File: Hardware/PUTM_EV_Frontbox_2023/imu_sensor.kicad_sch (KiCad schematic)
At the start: 21 parts, among them J5 Conn_01x06, J6 Conn_01x05, J7 Conn_01x02, J8 Conn_01x02, U17 IMS330DHCX, U2 AS5600

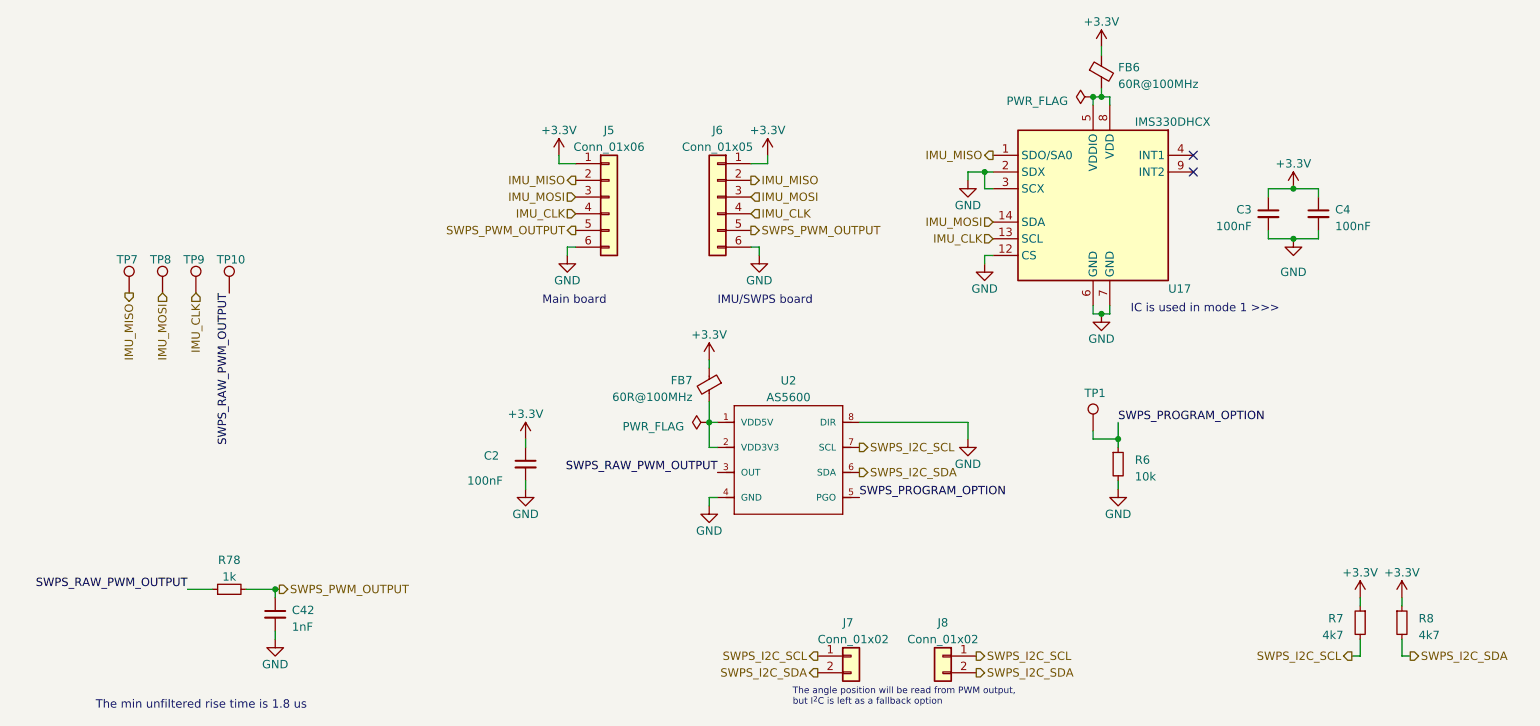
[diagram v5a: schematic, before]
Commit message: Schematic modified, footprints assigned
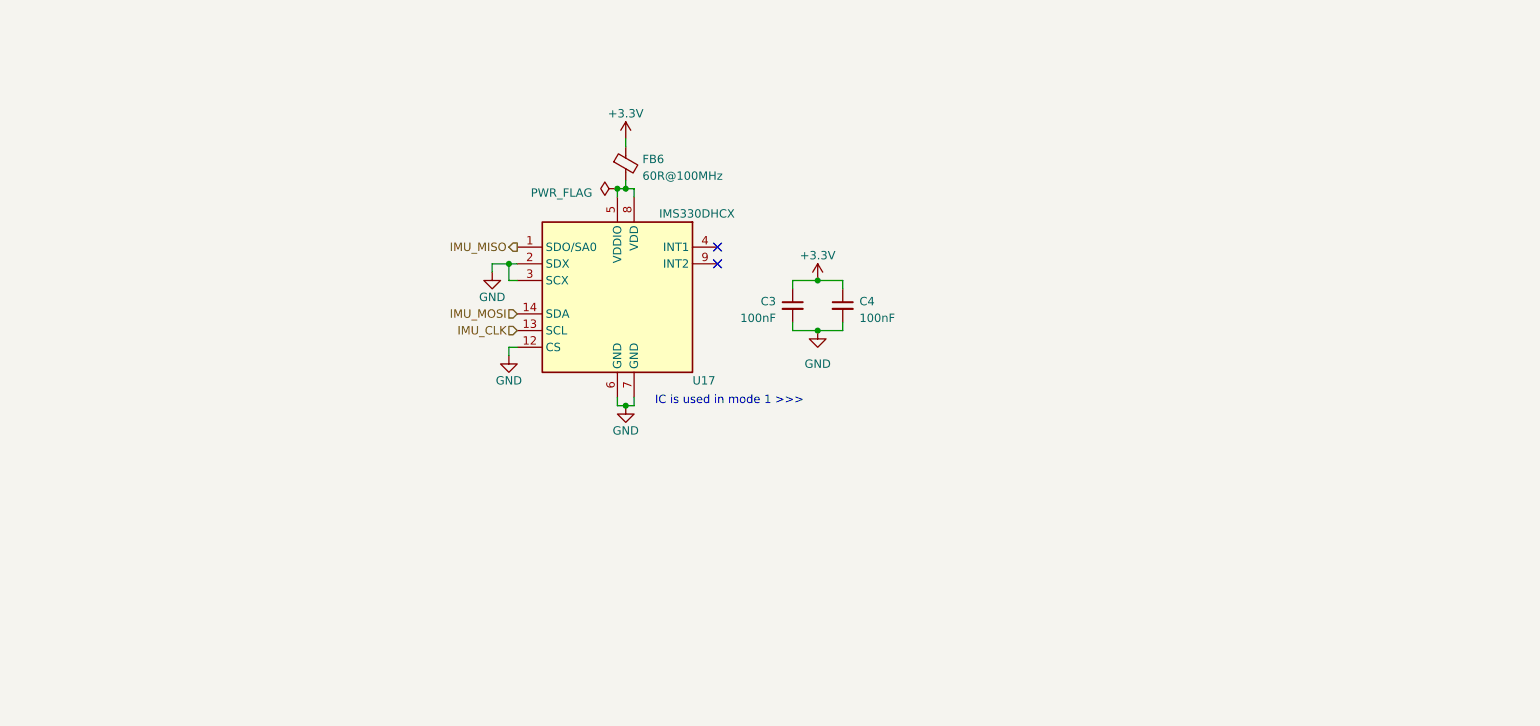
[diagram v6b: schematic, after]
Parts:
- removed C2: 100nF, symbol Device:C_Small
- removed C42: 1nF, symbol Device:C_Small
- removed FB7: 60R@100MHz, symbol Device:FerriteBead_Small
- removed J5: Conn_01x06, symbol Connector_Generic:Conn_01x06
- removed J6: Conn_01x05, symbol Connector_Generic:Conn_01x06
- removed J7, J8: Conn_01x02, symbol Connector_Generic:Conn_01x02
- removed R6: 10k, symbol Device:R_Small
- removed R7, R8: 4k7, symbol Device:R_Small
- removed R78: 1k, symbol Device:R_Small
- removed TP1, TP10, TP7, TP8, TP9: TestPoint, symbol Connector:TestPoint
- removed U2: AS5600, AS5600, symbol AS5600:AS5600
- C3, C4: footprint (none) -> Capacitor_SMD:C_0402_1005Metric_Pad0.74x0.62mm_HandSolder
- FB6: footprint (none) -> Inductor_SMD:L_0603_1608Metric
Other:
- note removed: "IMU/SWPS board"
- note removed: "Main board"
- note removed: "The angle position will be read from PWM output, but I^{2}C is left as a fallback option"
- note removed: "The min unfiltered rise time is 1.8 us"
- moved on the sheet: C3, C4, FB6, U17

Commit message: Grouped components
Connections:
- net +3.3V: no longer C3.1, C4.1
- net at FB6.2, U17.5 (VDDIO), U17.8 (VDD): now also C3.1, C4.1
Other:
- moved on the sheet: C3, C4
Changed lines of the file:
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@@
   (junction (at 109.22 76.2) (diameter 0) (color 0 0 0 0)
   )
-  (junction (at 139.7 97.79) (diameter 0) (color 0 0 0 0)
+  (junction (at 141.605 85.725) (diameter 0) (color 0 0 0 0)
   )
   (junction (at 92.71 87.63) (diameter 0) (color 0 0 0 0)
   )
-  (junction (at 139.7 90.17) (diameter 0) (color 0 0 0 0)
+  (junction (at 141.605 78.105) (diameter 0) (color 0 0 0 0)
   )
   (junction (at 110.49 109.22) (diameter 0) (color 0 0 0 0)
   )
+  (junction (at 111.76 76.2) (diameter 0) (color 0 0 0 0)
+  )
   (junction (at 110.49 76.2) (diameter 0) (color 0 0 0 0)
   )
@@
     (stroke (width 0) (type default))
   )
-  (wire (pts (xy 143.51 91.44) (xy 143.51 90.17))
+  (wire (pts (xy 145.415 79.375) (xy 145.415 78.105))
+    (stroke (width 0) (type default))
+  )
+  (wire (pts (xy 111.76 76.2) (xy 141.605 76.2))
     (stroke (width 0) (type default))
   )
@@
     (stroke (width 0) (type default))
   )
-  (wire (pts (xy 143.51 90.17) (xy 139.7 90.17))
+  (wire (pts (xy 137.795 78.105) (xy 141.605 78.105))
     (stroke (width 0) (type default))
   )
@@
     (stroke (width 0) (type default))
   )
-  (wire (pts (xy 143.51 97.79) (xy 139.7 97.79))
+  (wire (pts (xy 145.415 85.725) (xy 141.605 85.725))
     (stroke (width 0) (type default))
   )
-  (wire (pts (xy 110.49 76.2) (xy 111.76 76.2))
+  (wire (pts (xy 109.22 109.22) (xy 110.49 109.22))
     (stroke (width 0) (type default))
   )
-  (wire (pts (xy 109.22 109.22) (xy 110.49 109.22))
+  (wire (pts (xy 141.605 76.2) (xy 141.605 78.105))
     (stroke (width 0) (type default))
   )
@@
     (stroke (width 0) (type default))
   )
-  (wire (pts (xy 135.89 91.44) (xy 135.89 90.17))
+  (wire (pts (xy 137.795 79.375) (xy 137.795 78.105))
     (stroke (width 0) (type default))
   )
-  (wire (pts (xy 135.89 96.52) (xy 135.89 97.79))
+  (wire (pts (xy 137.795 84.455) (xy 137.795 85.725))
     (stroke (width 0) (type default))
   )
-  (wire (pts (xy 135.89 90.17) (xy 139.7 90.17))
+  (wire (pts (xy 110.49 76.2) (xy 111.76 76.2))
     (stroke (width 0) (type default))
   )
@@
     (stroke (width 0) (type default))
   )
-  (wire (pts (xy 143.51 96.52) (xy 143.51 97.79))
+  (wire (pts (xy 145.415 84.455) (xy 145.415 85.725))
+    (stroke (width 0) (type default))
+  )
+  (wire (pts (xy 141.605 78.105) (xy 145.415 78.105))
     (stroke (width 0) (type default))
   )
@@
     (stroke (width 0) (type default))
   )
-  (wire (pts (xy 135.89 97.79) (xy 139.7 97.79))
+  (wire (pts (xy 137.795 85.725) (xy 141.605 85.725))
     (stroke (width 0) (type default))
   )
@@
     )
   )
-  (symbol (lib_id "power:GND") (at 139.7 97.79 0) (unit 1)
+  (symbol (lib_id "power:GND") (at 141.605 85.725 0) (unit 1)
     (in_bom yes) (on_board yes) (dnp no) (fields_autoplaced)
-    (property "Reference" "#PWR032" (at 139.7 104.14 0)
+    (property "Reference" "#PWR032" (at 141.605 92.075 0)
       (effects (font (size 1.27 1.27)) hide)
     )
-    (property "Value" "GND" (at 139.7 102.87 0)
+    (property "Value" "GND" (at 141.605 90.805 0)
       (effects (font (size 1.27 1.27)))
     )
-    (property "Footprint" "" (at 139.7 97.79 0)
+    (property "Footprint" "" (at 141.605 85.725 0)
       (effects (font (size 1.27 1.27)) hide)
     )
-    (property "Datasheet" "" (at 139.7 97.79 0)
+    (property "Datasheet" "" (at 141.605 85.725 0)
       (effects (font (size 1.27 1.27)) hide)
     )
@@
     )
   )
-  (symbol (lib_id "power:+3.3V") (at 139.7 90.17 0) (unit 1)
-    (in_bom yes) (on_board yes) (dnp no) (fields_autoplaced)
-    (property "Reference" "#PWR031" (at 139.7 93.98 0)
-      (effects (font (size 1.27 1.27)) hide)
-    )
-    (property "Value" "+3.3V" (at 139.7 86.36 0)
-      (effects (font (size 1.27 1.27)))
-    )
-    (property "Footprint" "" (at 139.7 90.17 0)
-      (effects (font (size 1.27 1.27)) hide)
-    )
-    (property "Datasheet" "" (at 139.7 90.17 0)
-      (effects (font (size 1.27 1.27)) hide)
-    )
-    (pin "1")
-    (instances
-      (project "PUTM_EV_Frontbox_2023"
-        (path "/b652b05a-4e3d-4ad1-b032-18886abe7d45/fc1ffdcd-7b51-43f2-87c4-9a5d8609cd78"
-          (reference "#PWR031") (unit 1)
-        )
-      )
-    )
-  )
-  (symbol (lib_id "Device:C_Small") (at 135.89 93.98 0) (mirror y) (unit 1)
+  (symbol (lib_id "Device:C_Small") (at 137.795 81.915 0) (mirror y) (unit 1)
     (in_bom yes) (on_board yes) (dnp no)
-    (property "Reference" "C3" (at 133.35 93.3513 0)
+    (property "Reference" "C3" (at 135.255 81.2863 0)
       (effects (font (size 1.27 1.27)) (justify left))
     )
-    (property "Value" "100nF" (at 133.35 95.8913 0)
+    (property "Value" "100nF" (at 135.255 83.8263 0)
       (effects (font (size 1.27 1.27)) (justify left))
     )
-    (property "Footprint" "Capacitor_SMD:C_0402_1005Metric_Pad0.74x0.62mm_HandSolder" (at 135.89 93.98 0)
+    (property "Footprint" "Capacitor_SMD:C_0402_1005Metric_Pad0.74x0.62mm_HandSolder" (at 137.795 81.915 0)
       (effects (font (size 1.27 1.27)) hide)
     )
-    (property "Datasheet" "~" (at 135.89 93.98 0)
+    (property "Datasheet" "~" (at 137.795 81.915 0)
       (effects (font (size 1.27 1.27)) hide)
     )
@@
     )
   )
-  (symbol (lib_id "Device:C_Small") (at 143.51 93.98 0) (unit 1)
+  (symbol (lib_id "Device:C_Small") (at 145.415 81.915 0) (unit 1)
     (in_bom yes) (on_board yes) (dnp no)
-    (property "Reference" "C4" (at 146.05 93.3513 0)
+    (property "Reference" "C4" (at 147.955 81.2863 0)
       (effects (font (size 1.27 1.27)) (justify left))
     )
-    (property "Value" "100nF" (at 146.05 95.8913 0)
+    (property "Value" "100nF" (at 147.955 83.8263 0)
       (effects (font (size 1.27 1.27)) (justify left))
     )
-    (property "Footprint" "Capacitor_SMD:C_0402_1005Metric_Pad0.74x0.62mm_HandSolder" (at 143.51 93.98 0)
+    (property "Footprint" "Capacitor_SMD:C_0402_1005Metric_Pad0.74x0.62mm_HandSolder" (at 145.415 81.915 0)
       (effects (font (size 1.27 1.27)) hide)
     )
-    (property "Datasheet" "~" (at 143.51 93.98 0)
+    (property "Datasheet" "~" (at 145.415 81.915 0)
       (effects (font (size 1.27 1.27)) hide)
     )
